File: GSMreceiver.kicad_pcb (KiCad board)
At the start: 2 copper layers, 69 x 83 mm, 153 parts, among them J1 Relay_1, J10 SWD, J11 UART1, J12 DG390-5.0-02P, J2 Relay_2, J3 Relay_3, J4 Relay_4, J5 RF Antenna, J6 USB-C, J7 RS485, J8 1042240820, J9 1042240820, Q1 BC848, Q2 BC848, SW1 SM5-180UP-1, U1 PRAB34S, U10 STM32L072CBT6, U2 PRAB34S, U3 PRAB34S, U4 PRAB34S, U5 AP63203WU, U6 AP63200WU, U7 SIM800C-DS, U8 USBLC6-2SC6, U9 XR3072XIDTR-F, Y1 4 MHz, Y2 32768 kHz

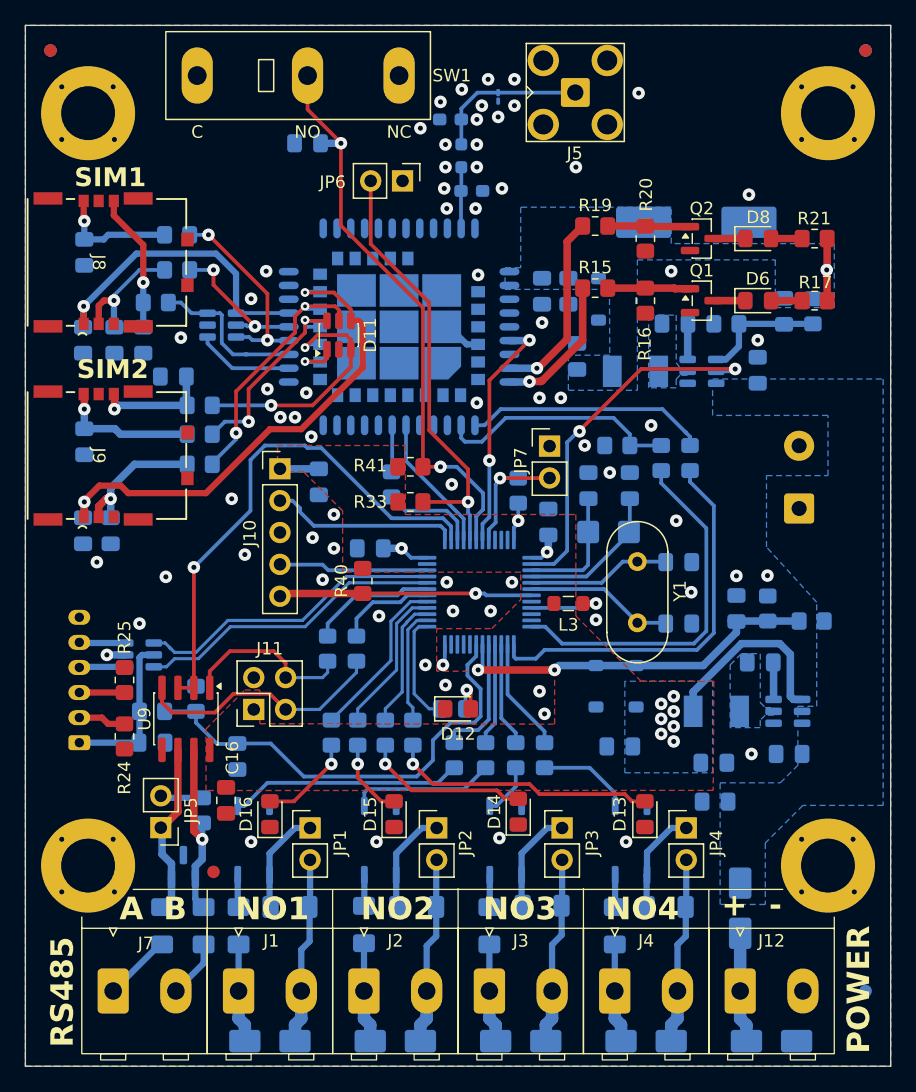
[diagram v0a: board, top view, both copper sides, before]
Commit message: Dual SIM version
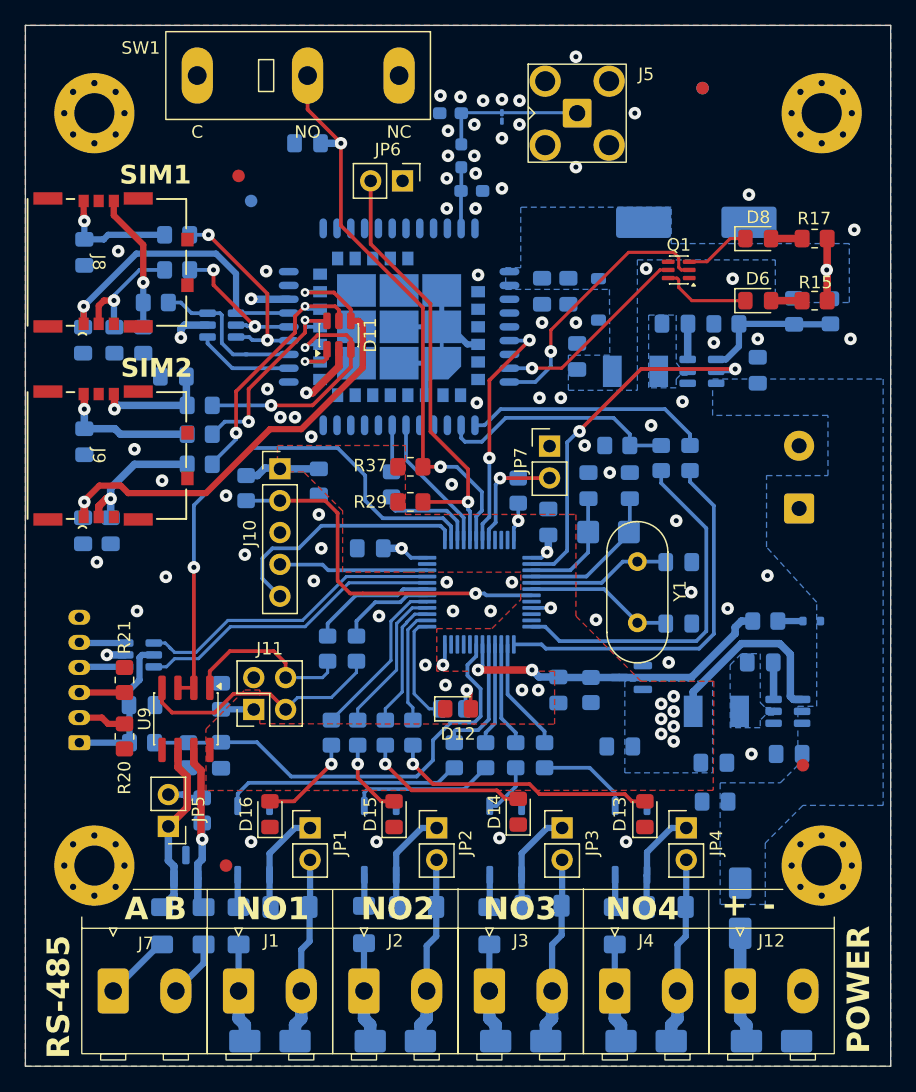
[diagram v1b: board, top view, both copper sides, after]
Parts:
- removed L3: MLZ2012M100WT000, Inductor_SMD:L_0805_2012Metric_Pad1.05x1.20mm_HandSolder
- removed Q2: BC848, Package_TO_SOT_SMD:SOT-23
- removed the R15 at (73.4, 44.0)
- removed the R16 at (77.4, 45.0)
- removed the R19 at (73.4, 39.0)
- removed the R20 at (77.4, 40.0)
- C16, FID1, FID2: moved to B.Cu
- D12, D13, D14, D15: value FYLS-0805PGC -> FYLS-0805GC
- D16: value FYLS-0805URC -> FYLS-0805SRC
- D17: value MBR0580 -> BAS40-04; footprint Diode_SMD:D_SOD-123 -> Package_TO_SOT_SMD:SOT-23
- D18: value MBR0580 -> 1N4148WT; footprint Diode_SMD:D_SOD-123 -> Diode_SMD:D_SOD-523
- FID4, FID5, FID6: moved to F.Cu
- H1, H2, H3, H4: footprint MountingHole:MountingHole_4.3mm_M4_DIN965_Pad -> MountingHole:MountingHole_3.2mm_M3_Pad_Via
- Q1: value BC848 -> MUN5233DW1; footprint Package_TO_SOT_SMD:SOT-23 -> Package_TO_SOT_SMD:SOT-363_SC-70-6
- R30: renamed from R34; value 680 -> 330
- R31: renamed from R35; value 680 -> 330
- R32: renamed from R36; value 680 -> 330
- R33: renamed from R37; value 680 -> 330
- R35: renamed from R39; value 680 -> 510
- R36: renamed from R40; moved to B.Cu
- moved FID4 21.4 mm to (90.0, 82.0), turned to 0 degrees
- moved FID1 20.3 mm to (46.0, 37.0), turned to 180 degrees
- moved FID5 18.0 mm to (45.0, 35.0), turned to 0 degrees
- moved D18 18.0 mm to (90.7, 70.5), turned to 0 degrees
- moved C34 15.6 mm to (70.5, 76.0), turned to 90 degrees
- moved R40 15.5 mm to (73.1, 76.0), turned to -90 degrees
- moved FID2 13.6 mm to (82.0, 28.0), turned to 180 degrees
- moved FID6 13.3 mm to (82.0, 28.0), turned to 0 degrees
- moved R36 11.9 mm to (45.6, 59.9)
- moved C16 8.31 mm to (43.6, 76.5), turned to -90 degrees
- moved R18 4.54 mm to (41.0, 81.2), turned to -90 degrees
- moved R41 3.70 mm to (87.0, 70.5)
- moved C15 3.10 mm to (37.3, 77.2)
- moved Q1 3.06 mm to (80.1, 42.5), turned to 180 degrees
- moved R19 2.62 mm to (37.3, 80.2)
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- renumbered C35 to C34, C34 to C35, R17 to R15, R18 to R16, R21 to R17, R22 to R18, R23 to R19, R24 to R20, R25 to R21, R26 to R22, R27 to R23, R28 to R24, R29 to R25, R30 to R26, R31 to R27, R32 to R28, R33 to R29, R38 to R34, R41 to R37, R42 to R38, R43 to R39, R44 to R40, R45 to R41
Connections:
- D17 pad 1: +3V3 -> GNDD
- D17 pad 2: /BATTERY_LEVEL -> +3V3
- D18 pad 1: /BATTERY_LEVEL -> Net-(D18-K)
- D18 pad 2: GNDD -> /Power_3.3V (page 3)/VBAT_IN
- J10 pad 2: /MCU/SWCLK -> /MCU/NRST
- J10 pad 5: /MCU/NRST -> /MCU/SWCLK
- Q1 pad 1: Net-(Q1-B) -> GNDD
- Q1 pad 2: GNDD -> /RFmodule/STATUS
- Q1 pad 3: Net-(D6-K) -> Net-(D8-K)
- R41 pad 2: /Power_3.3V (page 3)/VBAT_IN -> Net-(D18-K)
- U10 pad 9: Net-(U10-VDDA) -> +3V3
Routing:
- net GNDD: track 6.57 -> 31.8 mm, vias 84 -> 77
- net /RFmodule/STATUS: track 11.4 -> 21.4 mm
- net /MCU/NRST: track 20.2 -> 29.2 mm
- net +3V3: track 30.4 -> 37.4 mm, vias 11 -> 12
- net Net-(Q2-B): track 6.58 -> 0.00 mm
- net Net-(Q1-B): track 6.58 -> 0.00 mm
- net Net-(U10-VDDA): track 6.33 -> 0.00 mm, vias 1 -> 0
- net /MCU/SWCLK: track 15.1 -> 20.2 mm
- net Net-(D6-K): track 2.54 -> 7.25 mm
- net /BATTERY_LEVEL: track 30.5 -> 26.2 mm
- net Net-(D8-K): track 2.54 -> 5.24 mm
- net /Power_4V/4V-FB: track 9.22 -> 11.3 mm
- net Net-(D18-K): track 0.00 -> 2.00 mm
- net /RS485_EN: track 41.6 -> 43.1 mm
- net Net-(D7-A2): track 12.5 -> 11.3 mm
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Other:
- board text added: "RS-485"
- board text removed: "RS485"
